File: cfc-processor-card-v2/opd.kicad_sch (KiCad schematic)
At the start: 91 parts, among them Q2 PMV45EN, Q3 DMP2240UDM, Q4 PMV45EN, Q5 MOSFET-PCH-SOT23-6, Q6 MOSFET-PCH-SOT23-6, U12 MIC842LYC5, U13 MIC842LYC5, U14 MAX4211FETE, U15 TPS62112, U16 MAX7310ATE

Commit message: Clean up CFC Processor Card from Scott's initial import which was Gerber identical to origianl EAGLE schematic. Interestingly, this version was already changed for the v2 backplane which is great. Align schematic to be more KiCAD like based off of the C3, rename a few things, remove some outdated OPD connections, import sch into pcb, clean up pcb detritus, and import DRU settings. No longer Gerber identicial, but it's now ready for further polishing for fabrication.
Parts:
- R53, R56, R57: value NP -> 1k
- R54, R55, R58, R65, R66, R67, R68, R69, R70: value NP -> 1k; now not fitted
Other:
- note removed: "1.2"
- note removed: "OreSat Power Enable (PEN)"
- note removed: "OreSat Star Tracker: OPD v4.1"
- company: (none) -> Portland State Aerospace Society
- title: (none) -> OreSat CFC Processor Card
- moved on the sheet: C32, C33, C34, C35, C36, C37, C38, C39, C44, D6, D7, D8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

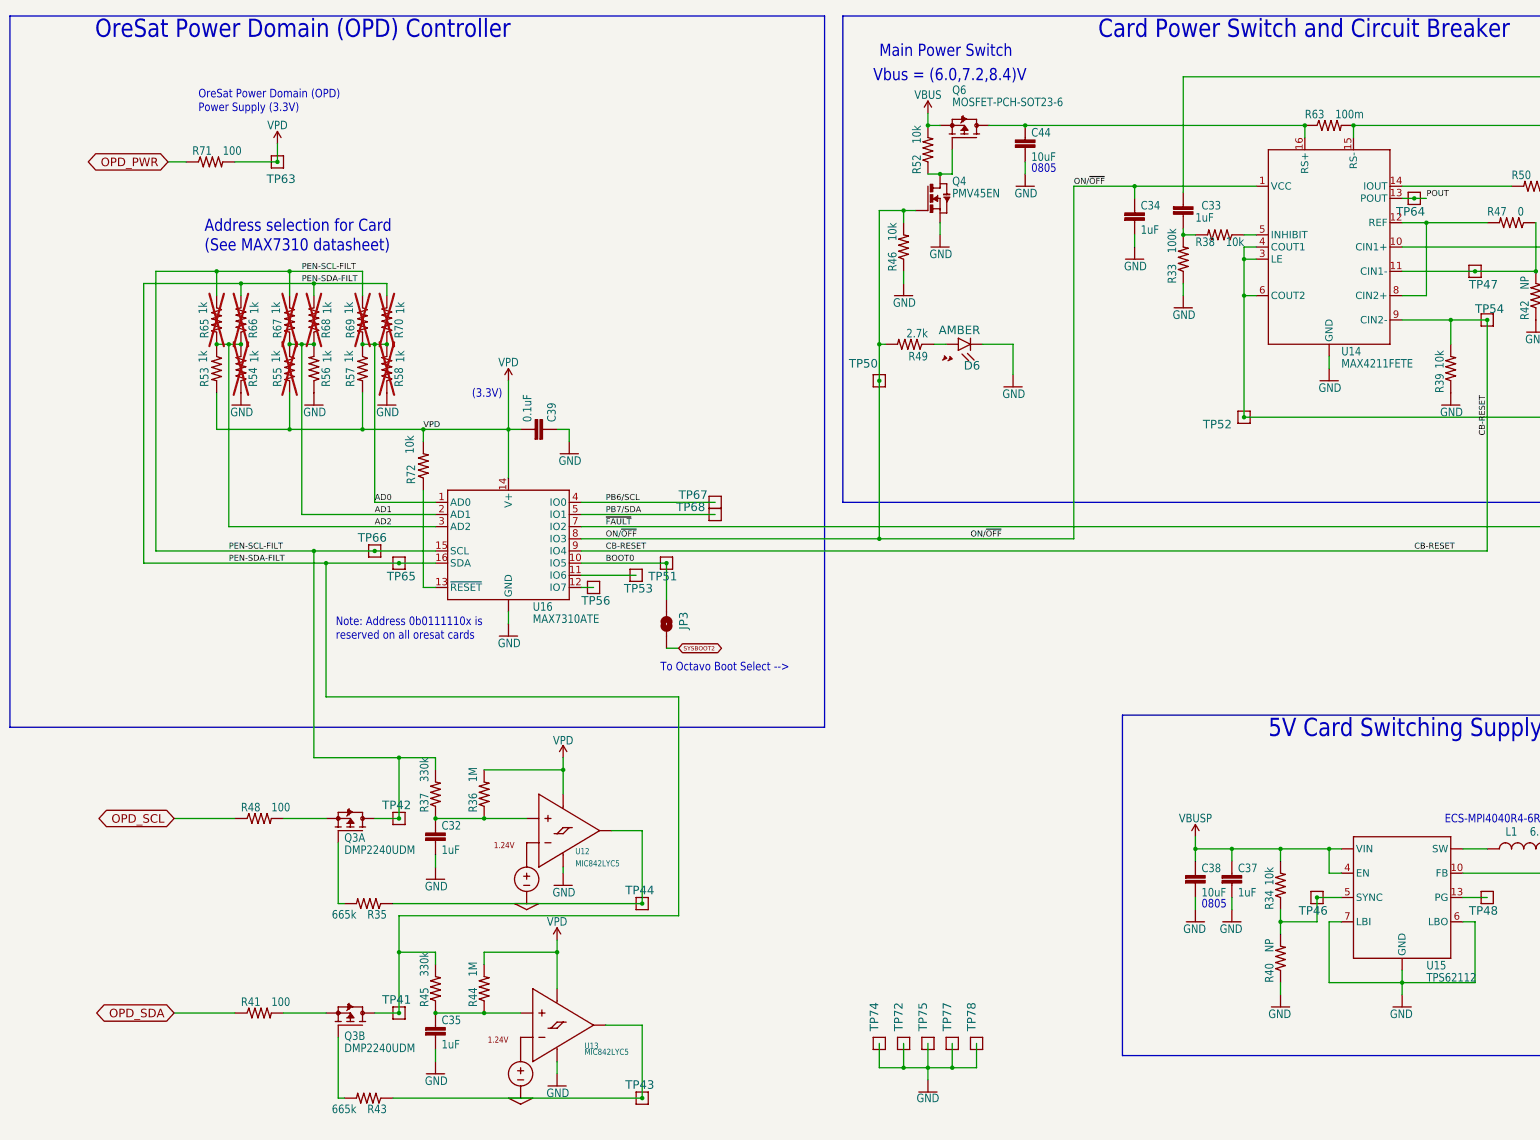
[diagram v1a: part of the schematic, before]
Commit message: Big cleanup - fixed a billion ERCs and DRCs. Switched a bunch of parts over to OreSat parts. Added analog switch on UART so CFC processor can talk serial to C3. Last thing left: clean up passives with new footprints, maybe.
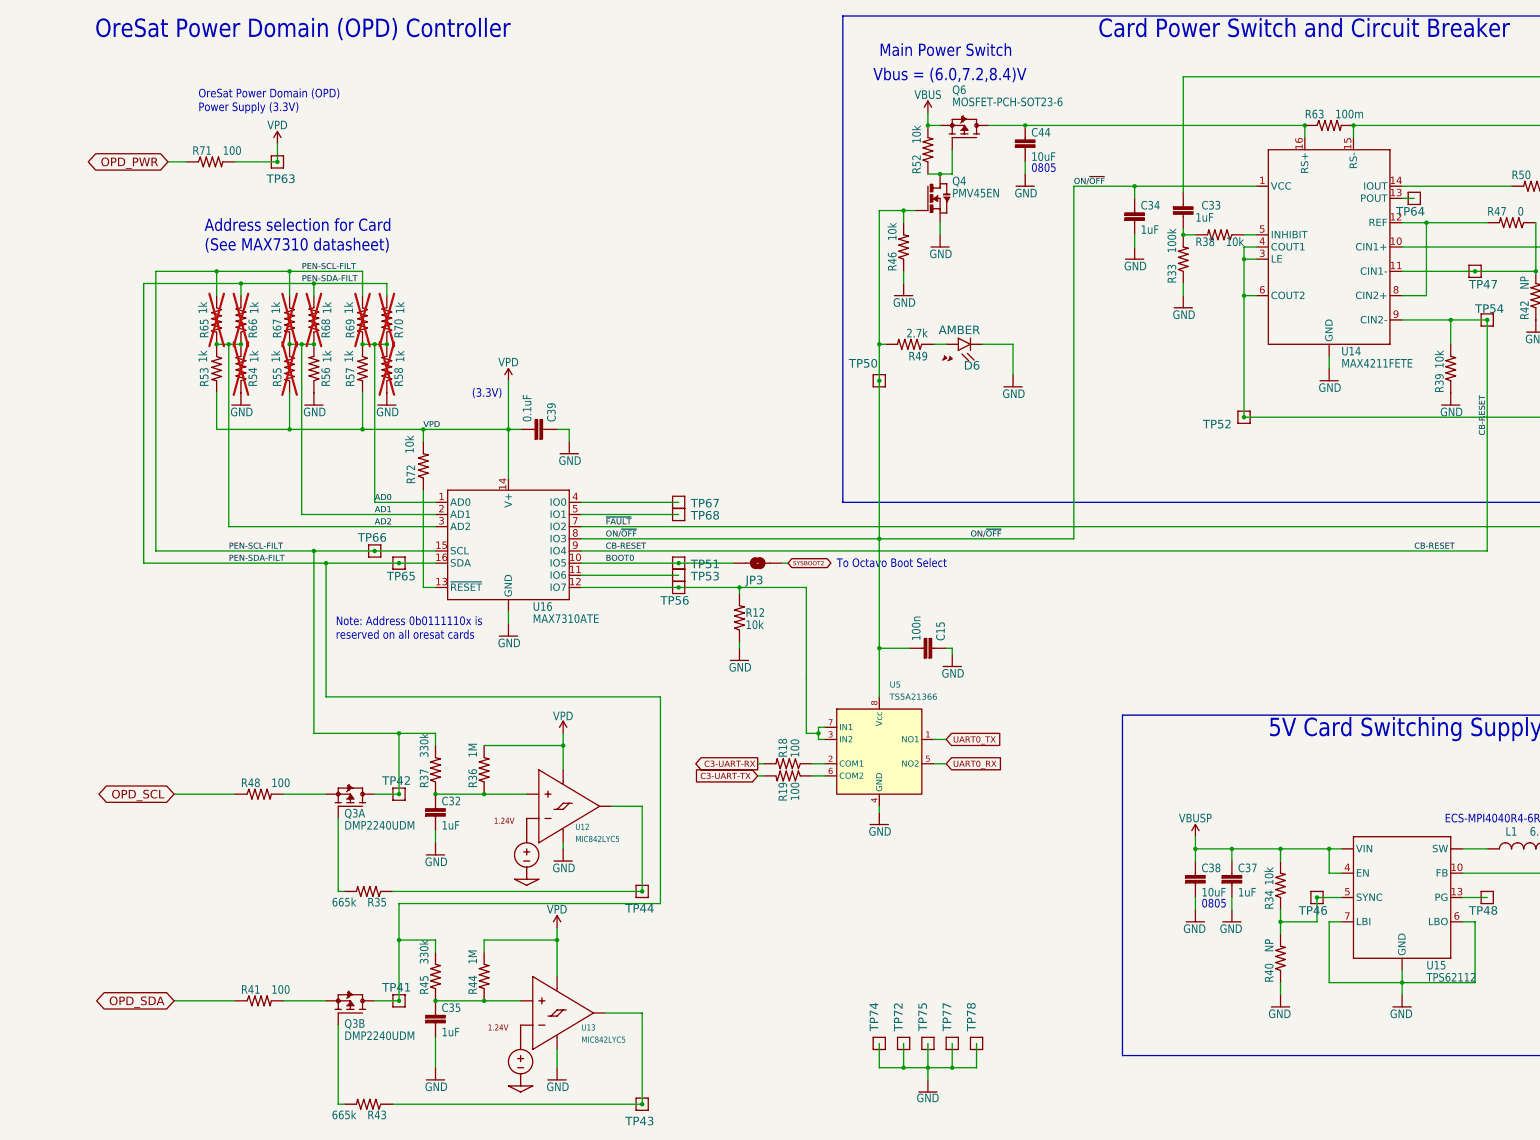
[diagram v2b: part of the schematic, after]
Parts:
- added C15: 100n, cfc-card:.0603-A, symbol cfc-card-eagle-import:C-EU0603-A
- added R12: 10k, cfc-card:.0603-A, symbol cfc-card-eagle-import:R-US_0603-A
- added R18, R19: 100, cfc-card:.0603-A, symbol cfc-card-eagle-import:R-US_0603-A
- added U5: TS5A21366, Package_SO:VSSOP-8_2.3x2mm_P0.5mm, symbol oresat-ics:TS5A21366
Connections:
- net GND: now also C15.1, R12.1, U5.4 (GND)
- net ON/~{OFF}: now also C15.2, U5.8 (Vcc)
- net at TP56.1, U16.12 (IO7): now also R12.2, U5.3 (IN2), U5.7 (IN1)
- net PB6/SCL: no longer names the net of TP67.1, U16.4 (IO0)
- net PB7/SDA: no longer names the net of TP68.1, U16.5 (IO1)
- net POUT: no longer names the net of TP64.1, U14.13 (POUT)
- new net: R18.1, U5.2 (COM1)
- new net: R19.1, U5.6 (COM2)
- new net C3-UART-RX: R18.2
- new net C3-UART-TX: R19.2
- new net UART0_RX: U5.5 (NO2)
- new net UART0_TX: U5.1 (NO1)
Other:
- note added: "To Octavo Boot Select"
- note removed: "To Octavo Boot Select -->"
- moved on the sheet: C32, C35, JP3, Q3A, Q3B, R35, R36, R37, R41, R43, R44, R45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

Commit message: more trace polishing.
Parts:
- C15, C33, C34, C37, C39, R12, R18, R19, R32, R33, R34, R35, R36, R37, R38, R39, R40, R41, R42, R43, R44, R45, R46, R47, R48, R49, R50, R51, R52, R53, R54, R55, R56, R57, R58, R61, R62, R64, R65, R66, R67, R68, R69, R70, R71, R72: footprint cfc-card:.0603-A -> oresat-passives:0603-C-NOSILK
- C32, C35: footprint cfc-card:.0805-B-NOSILK -> oresat-passives:0805-C-NOSILK
- C38, C44: footprint cfc-card:.0805-B -> oresat-passives:0805-C-NOSILK
- R63: footprint cfc-card:R1206_334 -> oresat-passives:1206-C
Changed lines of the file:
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@@
 			)
 		)
-		(property "Footprint" "cfc-card:.0603-A"
+		(property "Footprint" "oresat-passives:0603-C-NOSILK"
 			(at 123.19 175.26 0)
 			(effects
@@
 			)
 		)
-		(property "Footprint" "cfc-card:.0603-A"
+		(property "Footprint" "oresat-passives:0603-C-NOSILK"
 			(at 215.9 45.72 0)
 			(effects
@@
 			)
 		)
-		(property "Footprint" "cfc-card:.0603-A"
+		(property "Footprint" "oresat-passives:0603-C-NOSILK"
 			(at 353.06 58.42 0)
 			(effects
@@
 			)
 		)
-		(property "Footprint" "cfc-card:.0603-A"
+		(property "Footprint" "oresat-passives:0603-C-NOSILK"
 			(at 370.84 195.58 0)
 			(effects
@@
 			)
 		)
-		(property "Footprint" "cfc-card:.0603-A"
+		(property "Footprint" "oresat-passives:0603-C-NOSILK"
 			(at 76.2 180.34 0)
 			(effects
@@
 			)
 		)
-		(property "Footprint" "cfc-card:.0603-A"
+		(property "Footprint" "oresat-passives:0603-C-NOSILK"
 			(at 110.49 111.76 0)
 			(effects
@@
 			)
 		)
-		(property "Footprint" "cfc-card:.0603-A"
+		(property "Footprint" "oresat-passives:0603-C-NOSILK"
 			(at 97.79 91.44 0)
 			(effects
@@
 			)
 		)
-		(property "Footprint" "cfc-card:.0603-A"
+		(property "Footprint" "oresat-passives:0603-C-NOSILK"
 			(at 342.9 53.34 0)
 			(effects
@@
 			)
 		)
-		(property "Footprint" "cfc-card:.0603-A"
+		(property "Footprint" "oresat-passives:0603-C-NOSILK"
 			(at 67.31 91.44 0)
 			(effects
@@
 			)
 		)
-		(property "Footprint" "cfc-card:.0603-A"
+		(property "Footprint" "oresat-passives:0603-C-NOSILK"
 			(at 87.63 91.44 0)
 			(effects
@@
 			)
 		)
-		(property "Footprint" "cfc-card:.0603-A"
+		(property "Footprint" "oresat-passives:0603-C-NOSILK"
 			(at 325.12 91.44 0)
 			(effects
@@
 			)
 		)
-		(property "Footprint" "cfc-card:.0603-A"
+		(property "Footprint" "oresat-passives:0603-C-NOSILK"
 			(at 67.31 81.28 0)
 			(effects
@@
 			)
 		)
-		(property "Footprint" "cfc-card:.0603-A"
+		(property "Footprint" "oresat-passives:0603-C-NOSILK"
 			(at 72.39 81.28 0)
 			(effects
@@
 			)
 		)
-		(property "Footprint" "cfc-card:.0603-A"
+		(property "Footprint" "oresat-passives:0603-C-NOSILK"
 			(at 289.56 214.63 0)
 			(effects
@@
 			)
 		)
-		(property "Footprint" "cfc-card:.0603-A"
+		(property "Footprint" "oresat-passives:0603-C-NOSILK"
 			(at 82.55 91.44 0)
 			(effects
@@
 			)
 		)
-		(property "Footprint" "cfc-card:.0805-B-NOSILK"
+		(property "Footprint" "oresat-passives:0805-C-NOSILK"
 			(at 113.03 182.88 0)
 			(effects
@@
 			)
 		)
-		(property "Footprint" "cfc-card:.0603-A"
+		(property "Footprint" "oresat-passives:0603-C-NOSILK"
 			(at 279.4 196.85 0)
 			(effects
@@
 			)
 		)
-		(property "Footprint" "cfc-card:.0603-A"
+		(property "Footprint" "oresat-passives:0603-C-NOSILK"
 			(at 82.55 81.28 0)
 			(effects
@@
 			)
 		)
-		(property "Footprint" "cfc-card:.0805-B"
+		(property "Footprint" "oresat-passives:0805-C-NOSILK"
 			(at 236.22 43.18 0)
 			(effects
@@
 			)
 		)
-		(property "Footprint" "cfc-card:.0603-A"
+		(property "Footprint" "oresat-passives:0603-C-NOSILK"
 			(at 97.79 81.28 0)
 			(effects
@@
 			)
 		)
-		(property "Footprint" "cfc-card:.0603-A"
+		(property "Footprint" "oresat-passives:0603-C-NOSILK"
 			(at 342.9 76.2 0)
 			(effects
@@
 			)
 		)
-		(property "Footprint" "cfc-card:R1206_334"
+		(property "Footprint" "oresat-passives:1206-C"
 			(at 299.72 40.64 0)
 			(effects
@@
 			)
 		)
-		(property "Footprint" "cfc-card:.0603-A"
+		(property "Footprint" "oresat-passives:0603-C-NOSILK"
 			(at 217.17 149.86 0)
 			(effects
@@
 			)
 		)
-		(property "Footprint" "cfc-card:.0603-A"
+		(property "Footprint" "oresat-passives:0603-C-NOSILK"
 			(at 289.56 199.39 0)
 			(effects
@@
 			)
 		)
-		(property "Footprint" "cfc-card:.0805-B"
+		(property "Footprint" "oresat-passives:0805-C-NOSILK"
 			(at 271.78 196.85 0)
 			(effects
@@
 			)
 		)
-		(property "Footprint" "cfc-card:.0603-A"
+		(property "Footprint" "oresat-passives:0603-C-NOSILK"
 			(at 176.53 143.51 0)
 			(effects
@@
 			)
 		)
-		(property "Footprint" "cfc-card:.0603-A"
+		(property "Footprint" "oresat-passives:0603-C-NOSILK"
 			(at 212.09 86.36 0)
 			(effects
@@
 			)
 		)
-		(property "Footprint" "cfc-card:.0603-A"
+		(property "Footprint" "oresat-passives:0603-C-NOSILK"
 			(at 76.2 223.52 0)
 			(effects
@@
 			)
 		)
-		(property "Footprint" "cfc-card:.0603-A"
+		(property "Footprint" "oresat-passives:0603-C-NOSILK"
 			(at 113.03 175.26 0)
 			(effects
@@
 			)
 		)
-		(property "Footprint" "cfc-card:.0603-A"
+		(property "Footprint" "oresat-passives:0603-C-NOSILK"
 			(at 337.82 60.96 0)
 			(effects
@@
 			)
 		)
-		(property "Footprint" "cfc-card:.0603-A"
+		(property "Footprint" "oresat-passives:0603-C-NOSILK"
 			(at 99.06 245.11 0)
 			(effects
@@
 			)
 		)
-		(property "Footprint" "cfc-card:.0603-A"
+		(property "Footprint" "oresat-passives:0603-C-NOSILK"
 			(at 398.78 48.26 0)
 			(effects
@@
 			)
 		)
-		(property "Footprint" "cfc-card:.0603-A"
+		(property "Footprint" "oresat-passives:0603-C-NOSILK"
 			(at 102.87 81.28 0)
 			(effects
@@
 			)
 		)
-		(property "Footprint" "cfc-card:.0603-A"
+		(property "Footprint" "oresat-passives:0603-C-NOSILK"
 			(at 363.22 45.72 0)
 			(effects
@@
 			)
 		)
-		(property "Footprint" "cfc-card:.0603-A"
+		(property "Footprint" "oresat-passives:0603-C-NOSILK"
 			(at 102.87 91.44 0)
 			(effects
@@
 			)
 		)
-		(property "Footprint" "cfc-card:.0603-A"
+		(property "Footprint" "oresat-passives:0603-C-NOSILK"
 			(at 123.19 218.44 0)
 			(effects
@@
 			)
 		)
-		(property "Footprint" "cfc-card:.0603-A"
+		(property "Footprint" "oresat-passives:0603-C-NOSILK"
 			(at 375.92 60.96 0)
 			(effects
@@
 			)
 		)
-		(property "Footprint" "cfc-card:.0603-A"
+		(property "Footprint" "oresat-passives:0603-C-NOSILK"
 			(at 186.69 176.53 0)
 			(effects
@@
 			)
 		)
-		(property "Footprint" "cfc-card:.0603-A"
+		(property "Footprint" "oresat-passives:0603-C-NOSILK"
 			(at 135.89 104.14 0)
 			(effects
@@
 			)
 		)
-		(property "Footprint" "cfc-card:.0603-A"
+		(property "Footprint" "oresat-passives:0603-C-NOSILK"
 			(at 186.69 173.99 0)
 			(effects
@@
 			)
 		)
-		(property "Footprint" "cfc-card:.0603-A"
+		(property "Footprint" "oresat-passives:0603-C-NOSILK"
 			(at 269.24 68.58 0)
 			(effects
@@
 			)
 		)
-		(property "Footprint" "cfc-card:.0603-A"
+		(property "Footprint" "oresat-passives:0603-C-NOSILK"
 			(at 66.04 48.26 0)
 			(effects
@@
 			)
 		)
-		(property "Footprint" "cfc-card:.0603-A"
+		(property "Footprint" "oresat-passives:0603-C-NOSILK"
 			(at 99.06 200.66 0)
 			(effects
@@
 			)
 		)
-		(property "Footprint" "cfc-card:.0603-A"
+		(property "Footprint" "oresat-passives:0603-C-NOSILK"
 			(at 113.03 218.44 0)
 			(effects
@@
 			)
 		)
-		(property "Footprint" "cfc-card:.0603-A"
+		(property "Footprint" "oresat-passives:0603-C-NOSILK"
 			(at 87.63 81.28 0)
 			(effects
@@
 			)
 		)
-		(property "Footprint" "cfc-card:.0603-A"
+		(property "Footprint" "oresat-passives:0603-C-NOSILK"
 			(at 259.08 58.42 0)
 			(effects
@@
 			)
 		)
-		(property "Footprint" "cfc-card:.0603-A"
+		(property "Footprint" "oresat-passives:0603-C-NOSILK"
 			(at 276.86 63.5 0)
 			(effects
@@
 			)
 		)
-		(property "Footprint" "cfc-card:.0603-A"
+		(property "Footprint" "oresat-passives:0603-C-NOSILK"
 			(at 269.24 59.69 0)
 			(effects
@@
 			)
 		)
-		(property "Footprint" "cfc-card:.0603-A"
+		(property "Footprint" "oresat-passives:0603-C-NOSILK"
 			(at 72.39 91.44 0)
 			(effects
@@
 			)
 		)
-		(property "Footprint" "cfc-card:.0603-A"
+		(property "Footprint" "oresat-passives:0603-C-NOSILK"
 			(at 210.82 66.04 0)
 			(effects
@@
 			)
 		)
-		(property "Footprint" "cfc-card:.0805-B-NOSILK"
+		(property "Footprint" "oresat-passives:0805-C-NOSILK"
 			(at 113.03 226.06 0)
 			(effects
